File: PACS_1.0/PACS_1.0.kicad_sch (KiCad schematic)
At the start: 2 parts, among them U1 MSP430F5529, Y1 CSTNR4M00GH5L000R0

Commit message: Added New Sheets
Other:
- added sheet Actuators (PACS_1.0_actuators.kicad_sch)
- added sheet Power_USB (PACS_1.0_power.kicad_sch)
- added sheet Sensors (PACS_1.0_sensors.kicad_sch)
- company: (none) -> PACS
- title: (none) -> Main Sheet
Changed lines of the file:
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@@
 	(generator "eeschema")
 	(generator_version "8.0")
-	(paper "A4")
+	(paper "USLegal")
+	(title_block
+		(title "Main Sheet")
+		(rev "1.0")
+		(company "PACS")
+	)
 	(wire
 		(pts
@@
 				)
 			)
+		)
+	)
+	(sheet
+		(at 261.62 88.9)
+		(size 45.72 25.4)
+		(fields_autoplaced yes)
+		(stroke
+			(width 0.1524)
+			(type solid)
+		)
+		(fill
+			(color 0 0 0 0.0000)
+		)
+		(property "Sheetname" "Actuators"
+			(at 261.62 88.1884 0)
+			(effects
+				(font
+					(size 1.27 1.27)
+				)
+				(justify left bottom)
+			)
+		)
+		(property "Sheetfile" "PACS_1.0_actuators.kicad_sch"
+			(at 261.62 114.8846 0)
+			(effects
+				(font
+					(size 1.27 1.27)
+				)
+				(justify left top)
+			)
+		)
+		(instances
+			(project "PACS_1.0"
+				(path "/6996cbc8-fffb-40fd-8350-2bb7d19e6e7a"
+					(page "4")
+				)
+			)
+		)
+	)
+	(sheet
+		(at 223.52 43.18)
+		(size 50.8 35.56)
+		(fields_autoplaced yes)
+		(stroke
+			(width 0.1524)
+			(type solid)
+		)
+		(fill
+			(color 0 0 0 0.0000)
+		)
+		(property "Sheetname" "Sensors"
+			(at 223.52 42.4684 0)
+			(effects
+				(font
+					(size 1.27 1.27)
+				)
+				(justify left bottom)
+			)
+		)
+		(property "Sheetfile" "PACS_1.0_sensors.kicad_sch"
+			(at 223.52 79.3246 0)
+			(effects
+				(font
+					(size 1.27 1.27)
+				)
+				(justify left top)
+			)
+		)
+		(instances
+			(project "PACS_1.0"
+				(path "/6996cbc8-fffb-40fd-8350-2bb7d19e6e7a"
+					(page "3")
+				)
+			)
+		)
+	)
+	(sheet
+		(at 199.39 111.76)
+		(size 41.91 36.83)
+		(fields_autoplaced yes)
+		(stroke
+			(width 0.1524)
+			(type solid)
+		)
+		(fill
+			(color 0 0 0 0.0000)
+		)
+		(property "Sheetname" "Power_USB"
+			(at 199.39 111.0484 0)
+			(effects
+				(font
+					(size 1.27 1.27)
+				)
+				(justify left bottom)
+			)
+		)
+		(property "Sheetfile" "PACS_1.0_power.kicad_sch"
+			(at 199.39 149.1746 0)
+			(effects
+				(font
+					(size 1.27 1.27)
+				)
+				(justify left top)
+			)
+		)
+		(instances
+			(project "PACS_1.0"
+				(path "/6996cbc8-fffb-40fd-8350-2bb7d19e6e7a"
+					(page "2")
+				)
+			)

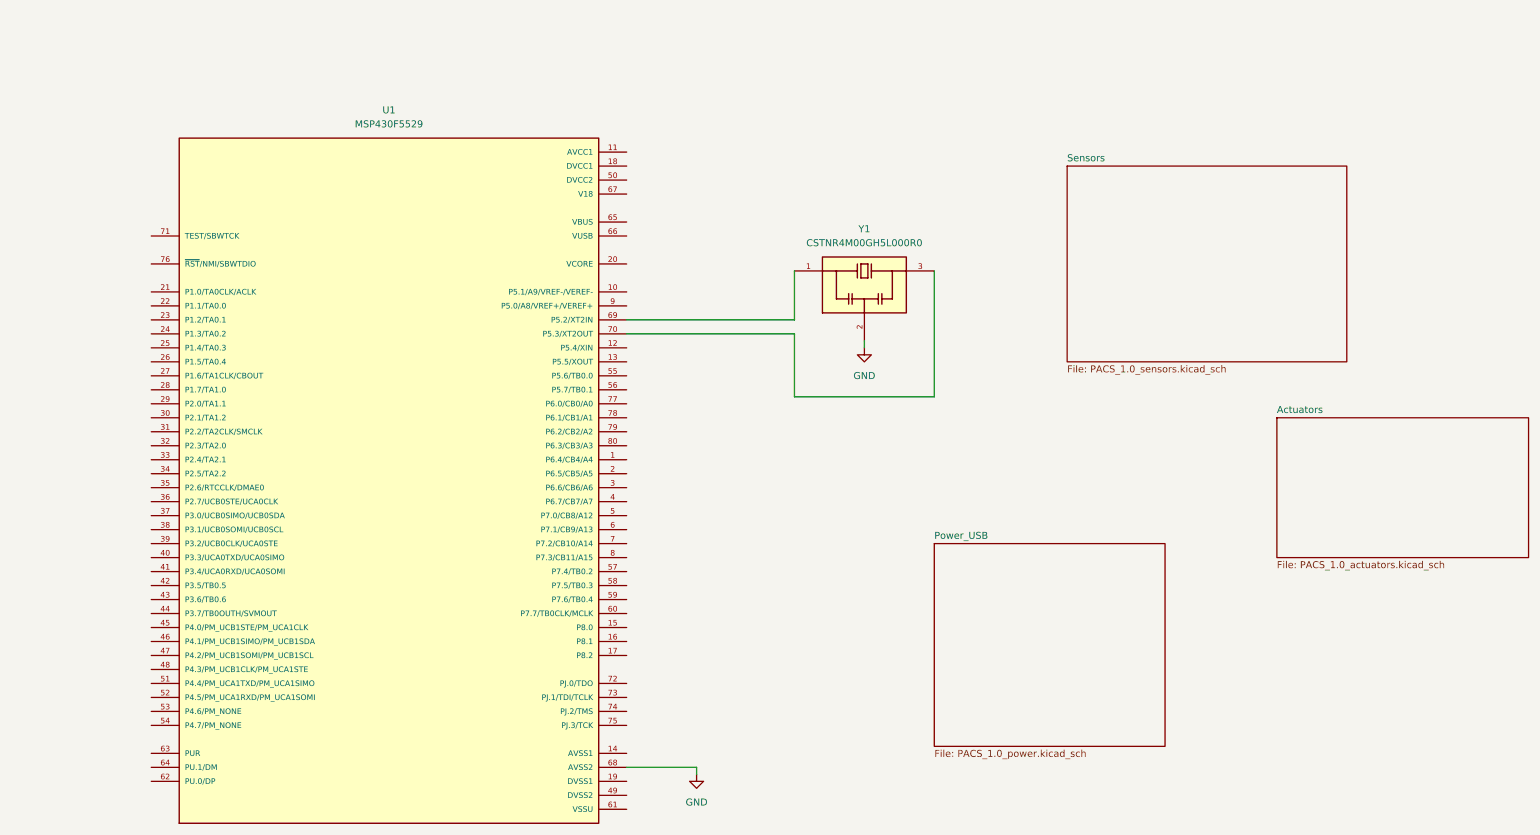
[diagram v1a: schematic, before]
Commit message: Added Bucks, Temp and Light Sensor
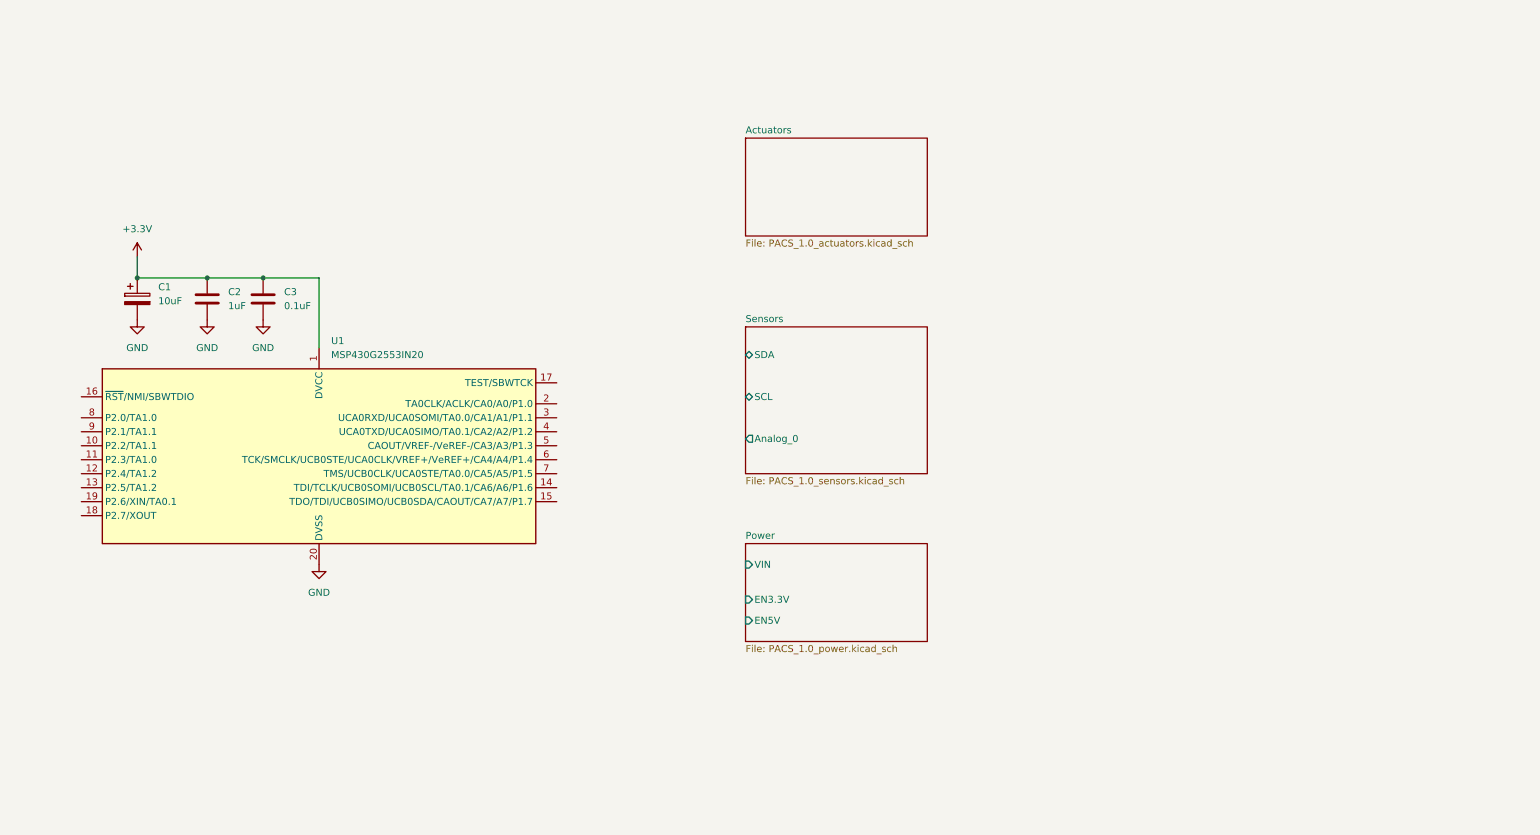
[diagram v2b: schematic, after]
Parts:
- removed U1: MSP430F5529, MSP430F5529:QFP50P1400X1400X160-80N, symbol MSP430F5529:MSP430F5529
- removed Y1: CSTNR4M00GH5L000R0, CSTNR4M00GH5L000R0:OSC_CSTNR4M00GH5L000R0, symbol CSTNR4M00GH5L000R0:CSTNR4M00GH5L000R0
- added C1: 10uF, symbol Device:C_Polarized
- added C2: 1uF, symbol Device:C
- added C3: 0.1uF, symbol Device:C
- added U1: MSP430G2553IN20, Package_DIP:DIP-20_W7.62mm, symbol MCU_Texas_MSP430:MSP430G2553IN20
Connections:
- net GND: now also C1.2, C2.2, C3.2, U1.20 (DVSS)
- new net +3.3V: C1.1, C2.1, C3.1, U1.1 (DVCC)
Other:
- sheet Power_USB renamed Power
- sheet Power ports: added EN3.3V, EN5V, VIN; removed none
- sheet Sensors ports: added Analog_0, SCL, SDA; removed none

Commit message: New Changes
We had the discussion about water pump, INA, LEDS, and battery solution. Not much changes from previous night.
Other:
- sheet Actuators renamed LEDS
- added sheet Water Pump (PACS_1.0_pump.kicad_sch)
- sheet LEDS: file PACS_1.0_actuators.kicad_sch -> PACS_1.0_leds.kicad_sch
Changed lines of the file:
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@@
+	)
+	(sheet
+		(at 220.98 38.1)
+		(size 26.67 15.24)
+		(fields_autoplaced yes)
+		(stroke
+			(width 0.1524)
+			(type solid)
+		)
+		(fill
+			(color 0 0 0 0.0000)
+		)
+		(property "Sheetname" "Water Pump"
+			(at 220.98 37.3884 0)
+			(effects
+				(font
+					(size 1.27 1.27)
+				)
+				(justify left bottom)
+			)
+		)
+		(property "Sheetfile" "PACS_1.0_pump.kicad_sch"
+			(at 220.98 53.9246 0)
+			(effects
+				(font
+					(size 1.27 1.27)
+				)
+				(justify left top)
+			)
+		)
+		(instances
+			(project "PACS_1.0"
+				(path "/6996cbc8-fffb-40fd-8350-2bb7d19e6e7a"
+					(page "5")
+				)
+			)
+		)
 	)
 	(sheet
@@
 			(color 0 0 0 0.0000)
 		)
-		(property "Sheetname" "Actuators"
+		(property "Sheetname" "LEDS"
 			(at 165.1 37.3884 0)
 			(effects
@@
 			)
 		)
-		(property "Sheetfile" "PACS_1.0_actuators.kicad_sch"
+		(property "Sheetfile" "PACS_1.0_leds.kicad_sch"
 			(at 165.1 56.4646 0)
 			(effects

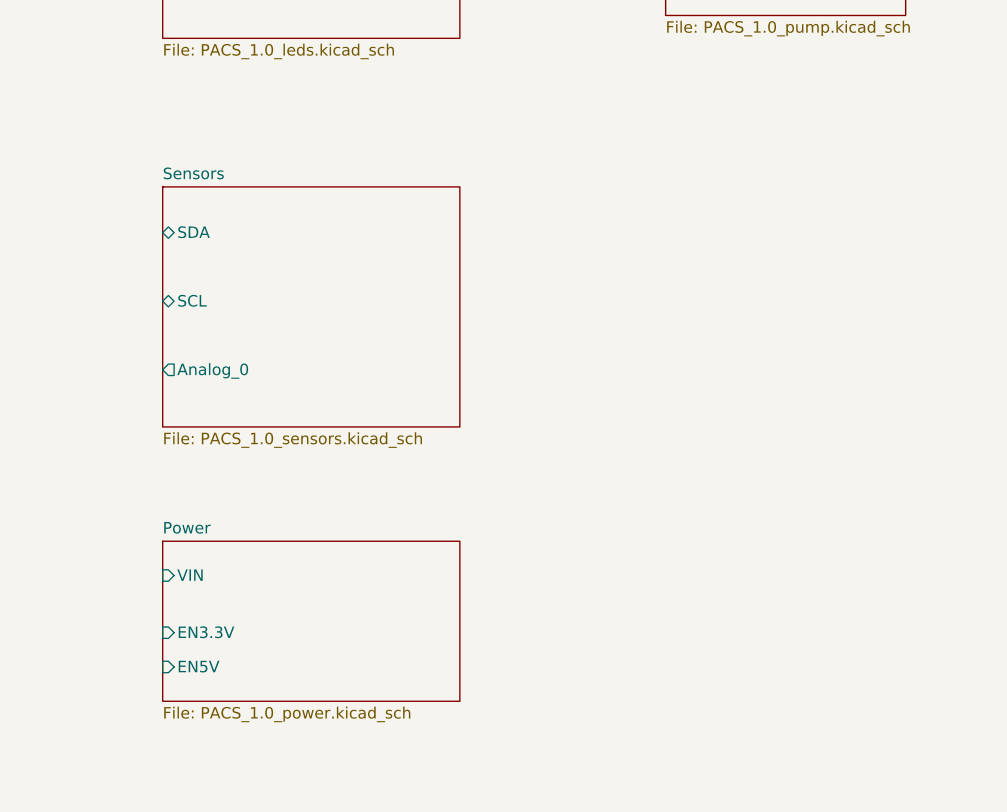
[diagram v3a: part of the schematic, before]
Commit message: Added Water level sensor and start of Pump
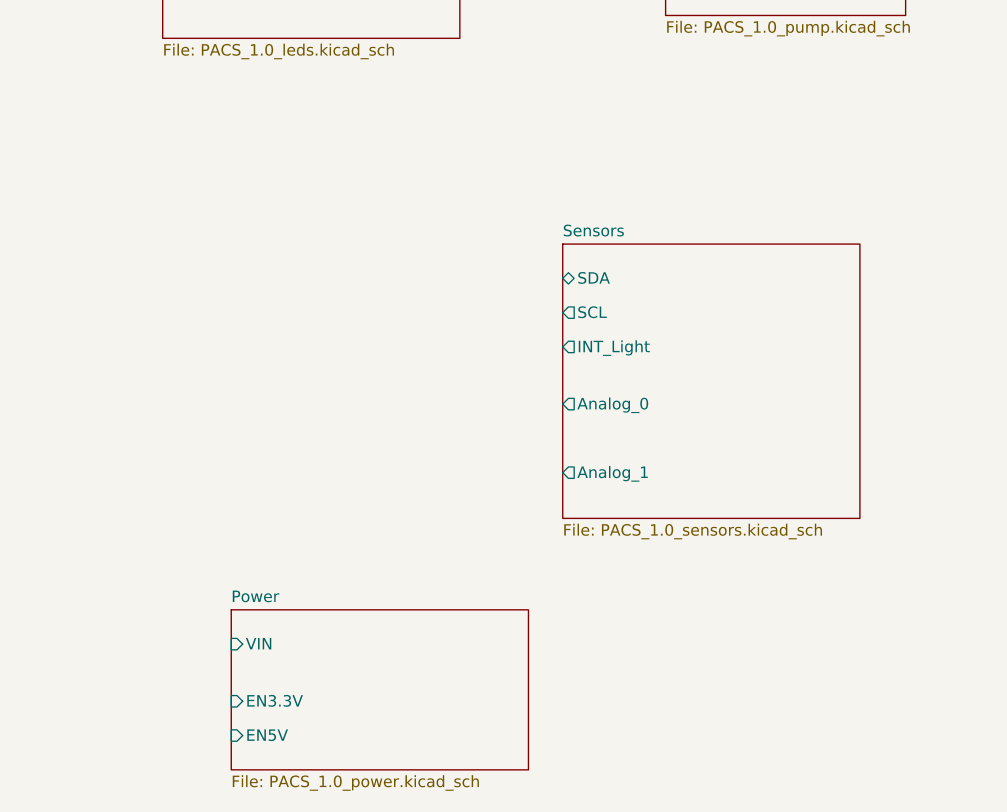
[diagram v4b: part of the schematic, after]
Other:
- sheet Sensors ports: added Analog_1, INT_Light; removed none
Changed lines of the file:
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@@
 	)
 	(sheet
-		(at 165.1 72.39)
-		(size 33.02 26.67)
+		(at 209.55 78.74)
+		(size 33.02 30.48)
 		(fields_autoplaced yes)
 		(stroke
@@
 		)
 		(property "Sheetname" "Sensors"
-			(at 165.1 71.6784 0)
+			(at 209.55 78.0284 0)
 			(effects
 				(font
@@
 		)
 		(property "Sheetfile" "PACS_1.0_sensors.kicad_sch"
-			(at 165.1 99.6446 0)
+			(at 209.55 109.8046 0)
 			(effects
 				(font
@@
 		)
 		(pin "SDA" bidirectional
-			(at 165.1 77.47 180)
+			(at 209.55 82.55 180)
 			(effects
 				(font
@@
 			)
 		)
-		(pin "SCL" bidirectional
-			(at 165.1 85.09 180)
+		(pin "SCL" output
+			(at 209.55 86.36 180)
 			(effects
 				(font
@@
 		)
 		(pin "Analog_0" output
-			(at 165.1 92.71 180)
+			(at 209.55 96.52 180)
+			(effects
+				(font
+					(size 1.27 1.27)
+				)
+				(justify left)
+			)
+		)
+		(pin "INT_Light" output
+			(at 209.55 90.17 180)
+			(effects
+				(font
+					(size 1.27 1.27)
+				)
+				(justify left)
+			)
+		)
+		(pin "Analog_1" output
+			(at 209.55 104.14 180)
 			(effects
 				(font
@@
 	)
 	(sheet
-		(at 165.1 111.76)
+		(at 172.72 119.38)
 		(size 33.02 17.78)
 		(fields_autoplaced yes)
@@
 		)
 		(property "Sheetname" "Power"
-			(at 165.1 111.0484 0)
+			(at 172.72 118.6684 0)
 			(effects
 				(font
@@
 		)
 		(property "Sheetfile" "PACS_1.0_power.kicad_sch"
-			(at 165.1 130.1246 0)
+			(at 172.72 137.7446 0)
 			(effects
 				(font
@@
 		)
 		(pin "EN5V" input
-			(at 165.1 125.73 180)
+			(at 172.72 133.35 180)
 			(effects
 				(font
@@
 		)
 		(pin "VIN" input
-			(at 165.1 115.57 180)
+			(at 172.72 123.19 180)
 			(effects
 				(font
@@
 		)
 		(pin "EN3.3V" input
-			(at 165.1 121.92 180)
+			(at 172.72 129.54 180)
 			(effects
 				(font
